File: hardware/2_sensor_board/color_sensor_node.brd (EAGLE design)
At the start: 27.9 x 30.5 mm, 19 parts, among them J1 JTAG, J2 JTAG, U1 ISL29125, U2 3.3V, U3 WS2811

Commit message: prepare for v10 generation
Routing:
- net DOUT: track 11.0 -> 8.35 mm
- net SCL: track 30.4 -> 32.2 mm
- net SDA: track 29.2 -> 30.8 mm
- net 5V: track 50.5 -> 49.4 mm
- net GND: vias 23 -> 25
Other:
- board text added: "SENSOR"
- board text added: "v10"
- board text removed: "v03"

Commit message: v10 CAM + Gerber Gen
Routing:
- net GND: vias 25 -> 24
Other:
- board text added: "ROUTE OUT"

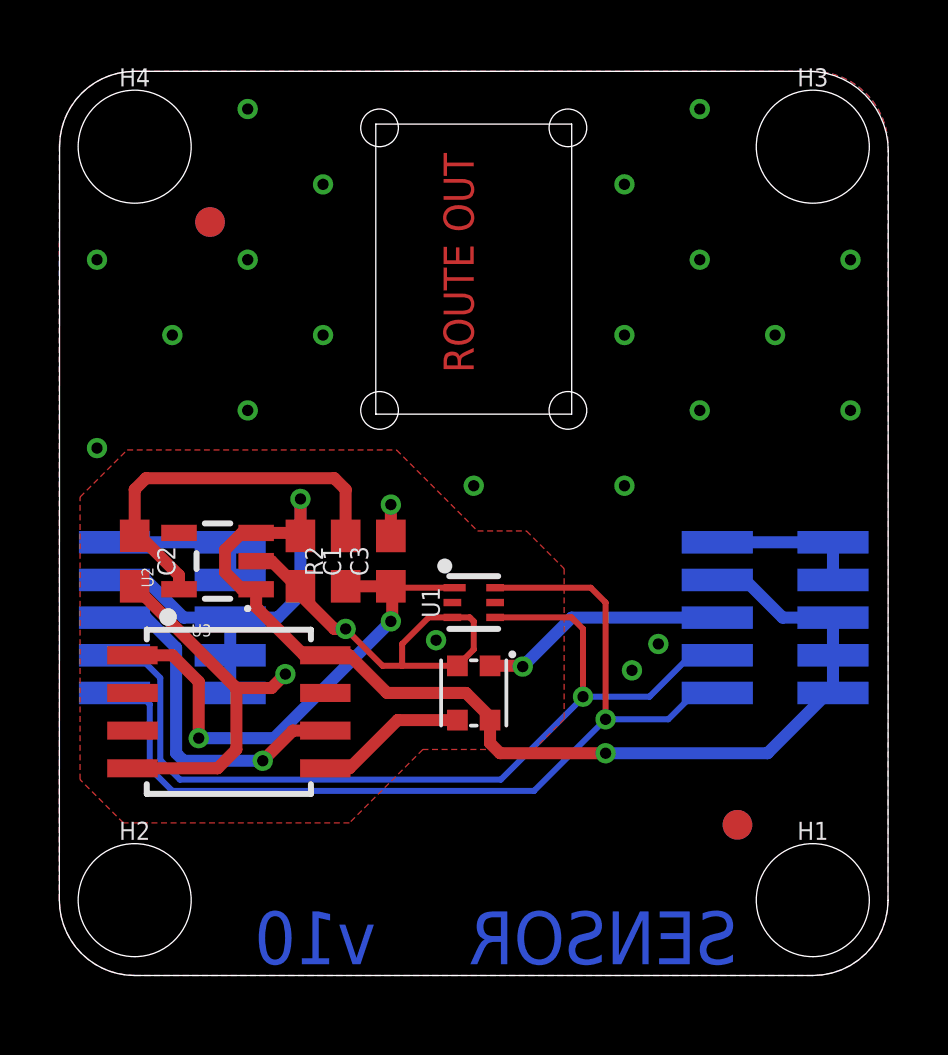
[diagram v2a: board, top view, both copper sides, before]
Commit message: increase width of shield
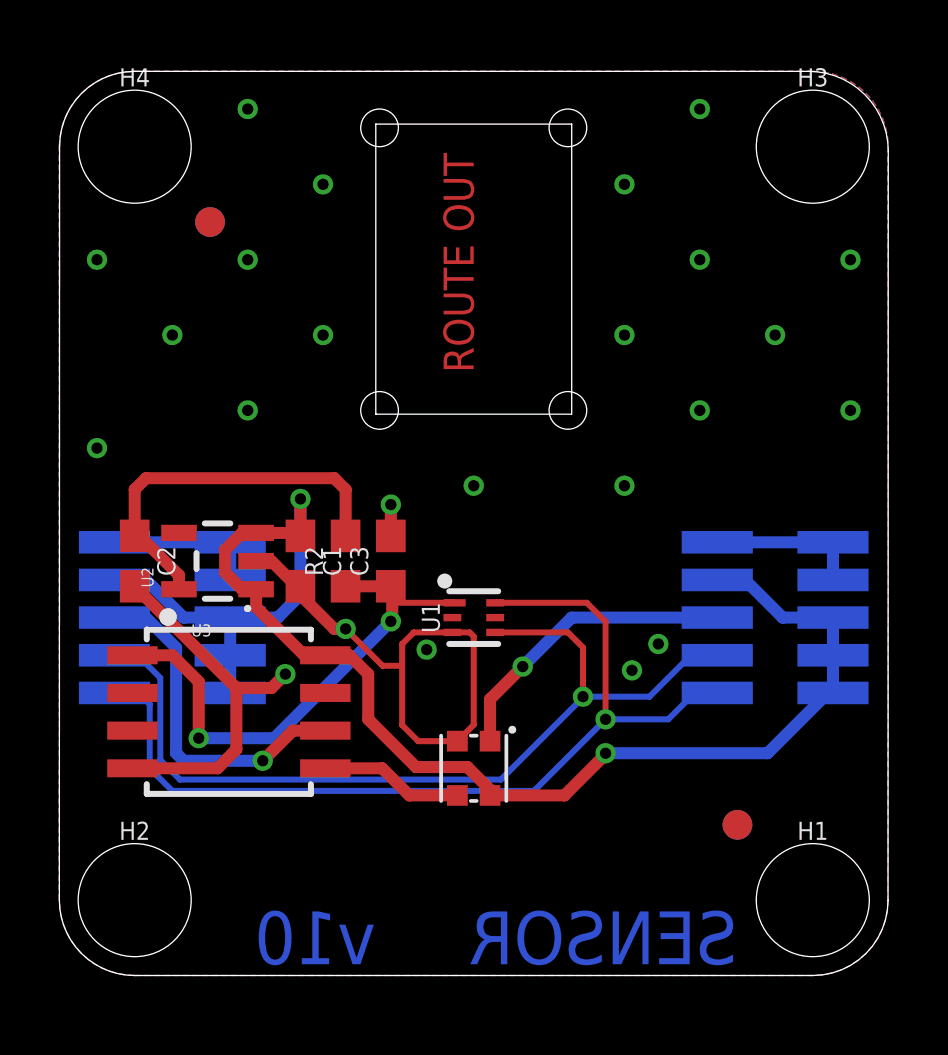
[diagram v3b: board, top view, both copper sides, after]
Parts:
- moved D1 2.54 mm to (14.0, 6.99)
- moved U1 0.51 mm to (14.0, 12.1)
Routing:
- net GND: track 37.7 -> 41.7 mm
- net DOUT: track 8.35 -> 10.2 mm
- net 5V: track 49.4 -> 51.1 mm
- net SCL: track 32.2 -> 31.6 mm
- net SDA: track 30.8 -> 30.3 mm
- net N$2: track 17.5 -> 17.0 mm
